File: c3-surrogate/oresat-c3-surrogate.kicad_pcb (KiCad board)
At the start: 2 copper layers, 99.8 x 94.6 mm, 72 parts, among them J1 J-SAMTEC-TFM-120-X1-XXX-D-RA, J2 Conn_01x04, J4 Conn_01x02_Socket, Q1 PMV45EN, Q3 NTR4101P, Q4 NTR2101P, Q5 DMP3050LVT-7, SW2 Slide Switch, SW3 OS203011MV9QS1, SW4 EG1218, U1 MAX892LEUA+T, U2 LTC4412xS6, U4 LTC4412xS6, U5 TS5A21366, U6 Trinket-M0

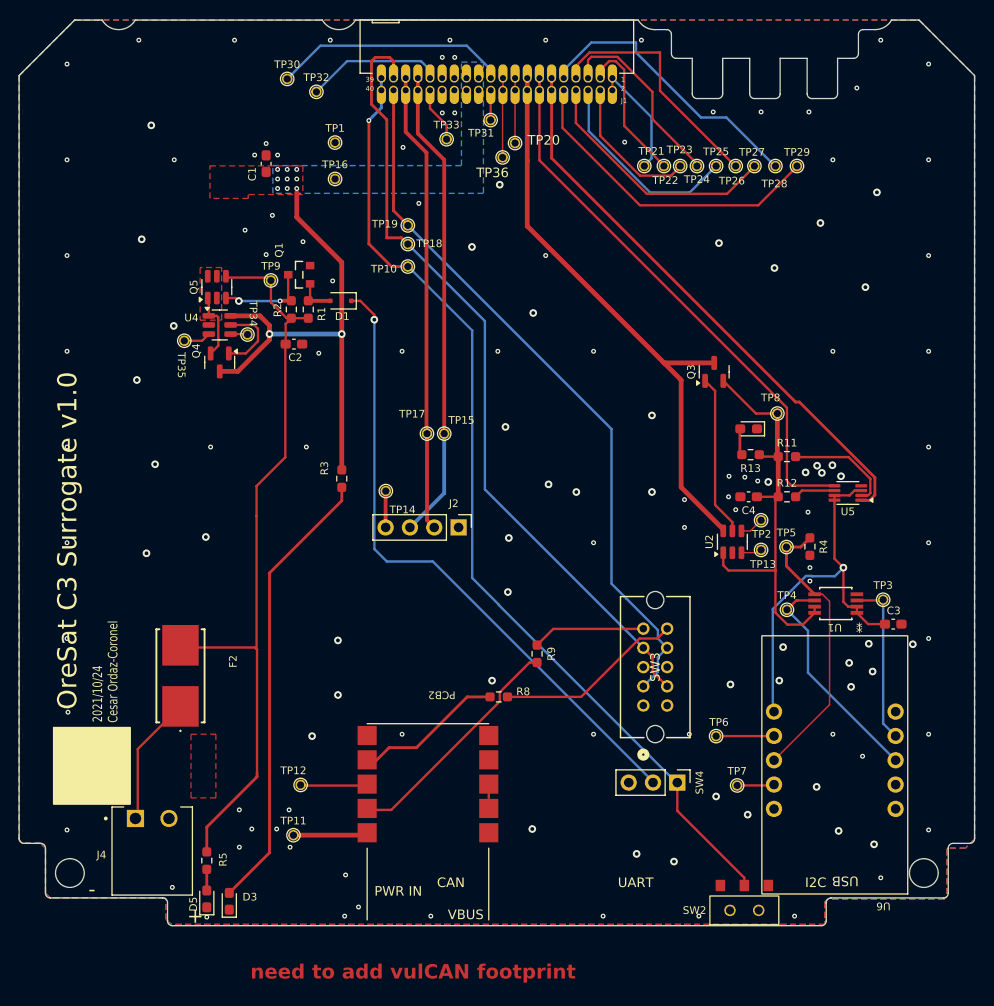
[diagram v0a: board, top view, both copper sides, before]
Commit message: made design review corrections to schematic and pcb
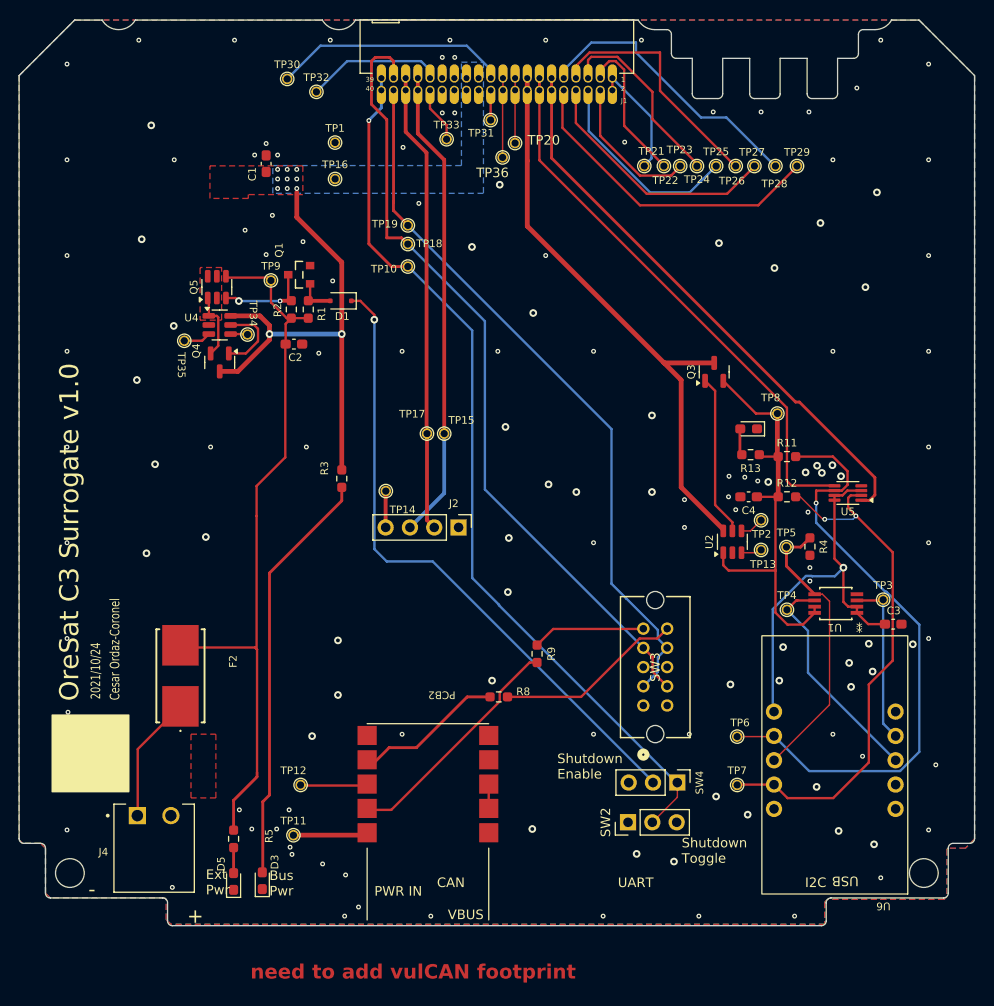
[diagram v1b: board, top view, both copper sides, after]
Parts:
- SW2: value Slide Switch -> EG1218; footprint S-CK-AYZ0102AGRLC-Slide-Switch:AYZ0102AGRLC -> Connector_PinHeader_2.54mm:PinHeader_1x03_P2.54mm_Vertical
- moved SW2 15.2 mm to (163.6, 139.2), turned to 90 degrees
- moved D3 4.07 mm to (125.4, 145.3)
- moved R5 3.60 mm to (122.4, 140.9)
- moved D5 3.34 mm to (122.4, 145.4)
- moved TP6 2.20 mm to (175.0, 130.2)
- moved J4 0.36 mm to (109.9, 146.5)
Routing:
- net Net-(U5-COM2): track 10.4 -> 64.3 mm, vias 0 -> 1
- net Net-(U5-COM1): track 15.2 -> 55.2 mm, vias 0 -> 2
- net ~{SD}: track 102.2 -> 93.8 mm
- net Net-(D3-A): track 47.2 -> 43.7 mm
- net Net-(Q5-S): track 79.0 -> 76.0 mm
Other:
- board text added: "Bus Pwr"
- board text added: "Ext Pwr"
- board text added: "Shutdown Enable"
- board text added: "Shutdown Toggle"

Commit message: edited via size, rearranged tracks
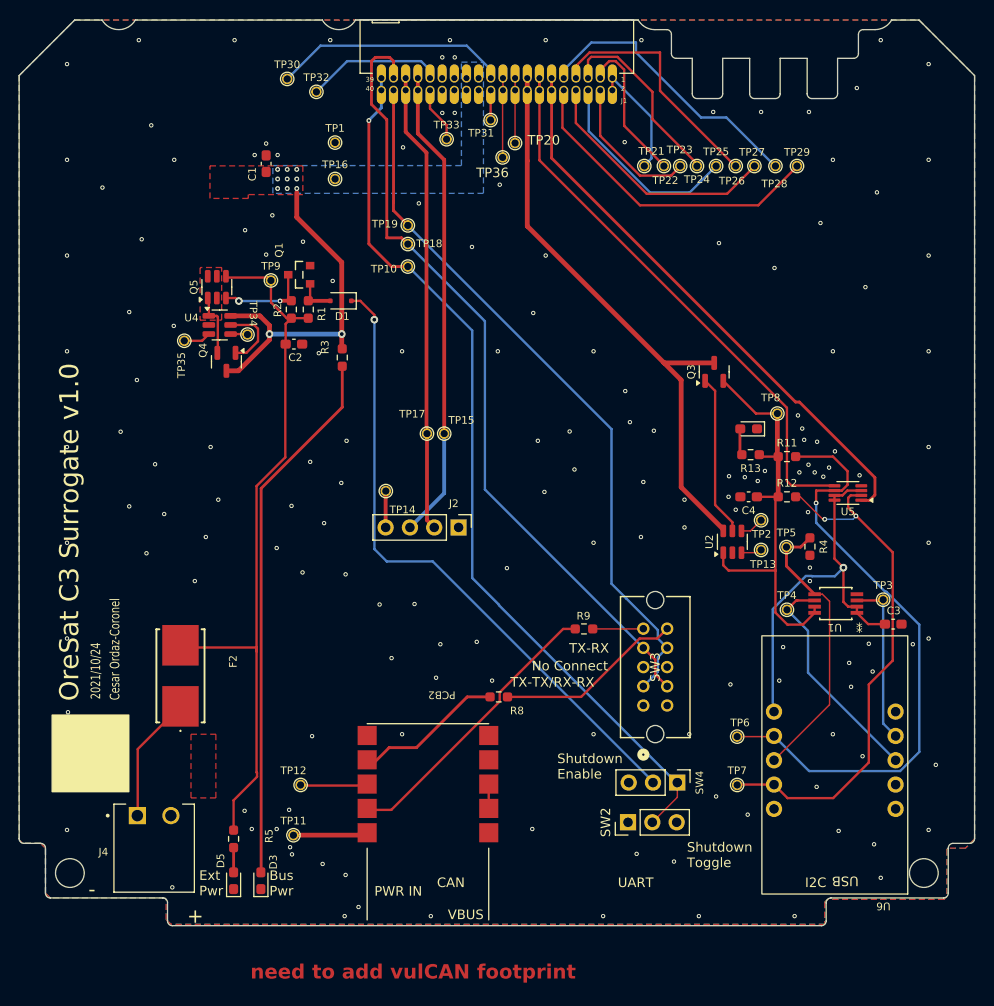
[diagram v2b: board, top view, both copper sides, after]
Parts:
- moved R3 12.7 mm to (133.8, 90.7)
- moved R9 5.55 mm to (159.0, 119.0), turned to 0 degrees
- moved Q4 0.70 mm to (121.7, 91.1)
- moved D3 0.15 mm to (125.2, 145.3)
- moved D5 0.08 mm to (122.4, 145.3)
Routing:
- net VBUS: track 51.0 -> 37.7 mm
- net Net-(D3-A): track 43.7 -> 56.4 mm
- net Net-(R9-Pad2): track 11.8 -> 5.30 mm
- net Net-(PCB2-RXD): track 24.7 -> 30.1 mm
- net Net-(Q4-G): track 7.91 -> 7.18 mm
- net GND: vias 134 -> 161
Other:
- board text added: "No Connect"
- board text added: "TX-RX"
- board text added: "TX-TX/RX-RX"

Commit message: fixed transistor that flipped
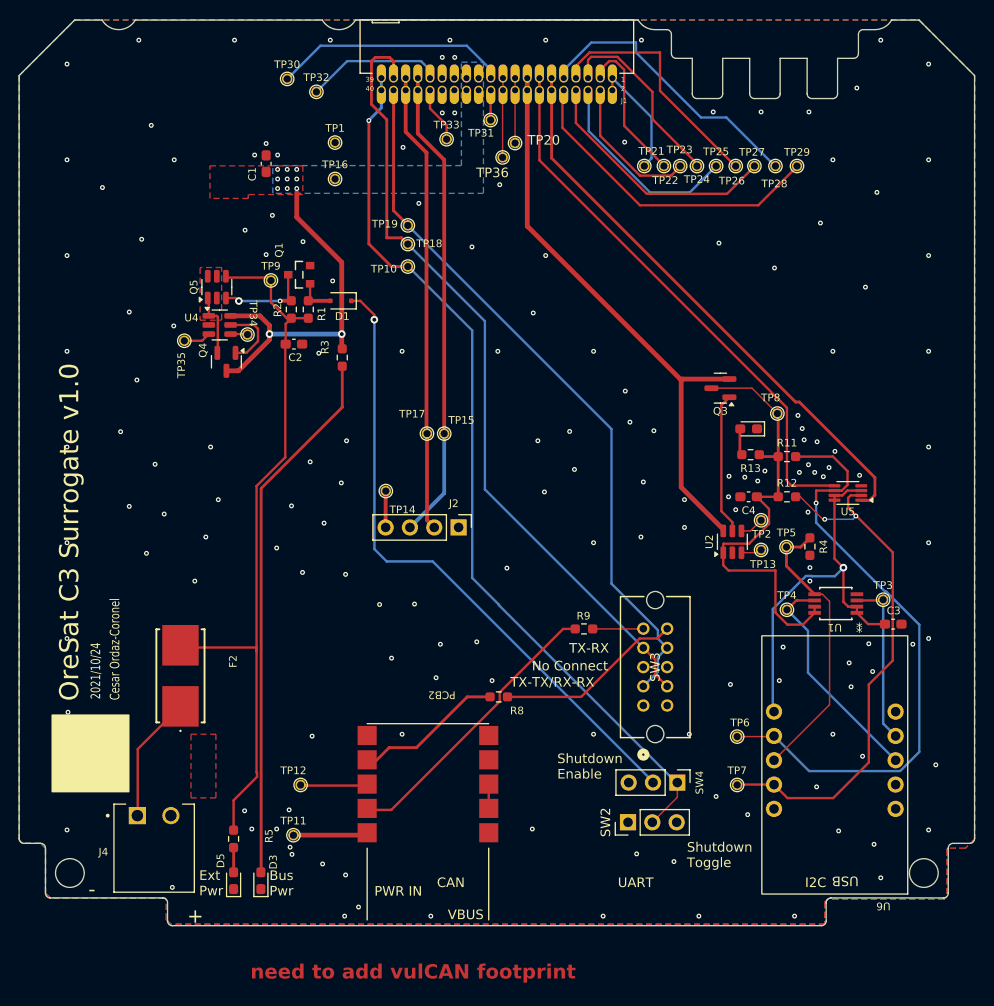
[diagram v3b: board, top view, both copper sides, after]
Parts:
- F2: value Fuse_Small -> 0155900DR
- Q4: value NTR2101P -> NTR4101P
- moved Q3 1.82 mm to (173.2, 93.8), turned to 180 degrees
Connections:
- C4 pad 1: Net-(Q3-S) -> Net-(Q3-D)
- Q3 pad 2: Net-(Q3-S) -> OPD_PWR
- Q3 pad 3: OPD_PWR -> Net-(Q3-D)
- R11 pad 1: Net-(Q3-S) -> Net-(Q3-D)
- R12 pad 1: Net-(Q3-S) -> Net-(Q3-D)
- R13 pad 1: Net-(Q3-S) -> Net-(Q3-D)
- TP8 pad 1: Net-(Q3-S) -> Net-(Q3-D)
- U1 pad 7: Net-(Q3-S) -> Net-(Q3-D)
- U1 pad 8: Net-(Q3-S) -> Net-(Q3-D)
- U2 pad 1: Net-(Q3-S) -> Net-(Q3-D)
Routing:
- net Net-(Q3-D): track 0.00 -> 48.6 mm
- net Net-(Q3-S): track 45.2 -> 0.00 mm
- net Net-(Q3-G): track 16.9 -> 14.8 mm

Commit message: added vulCAN
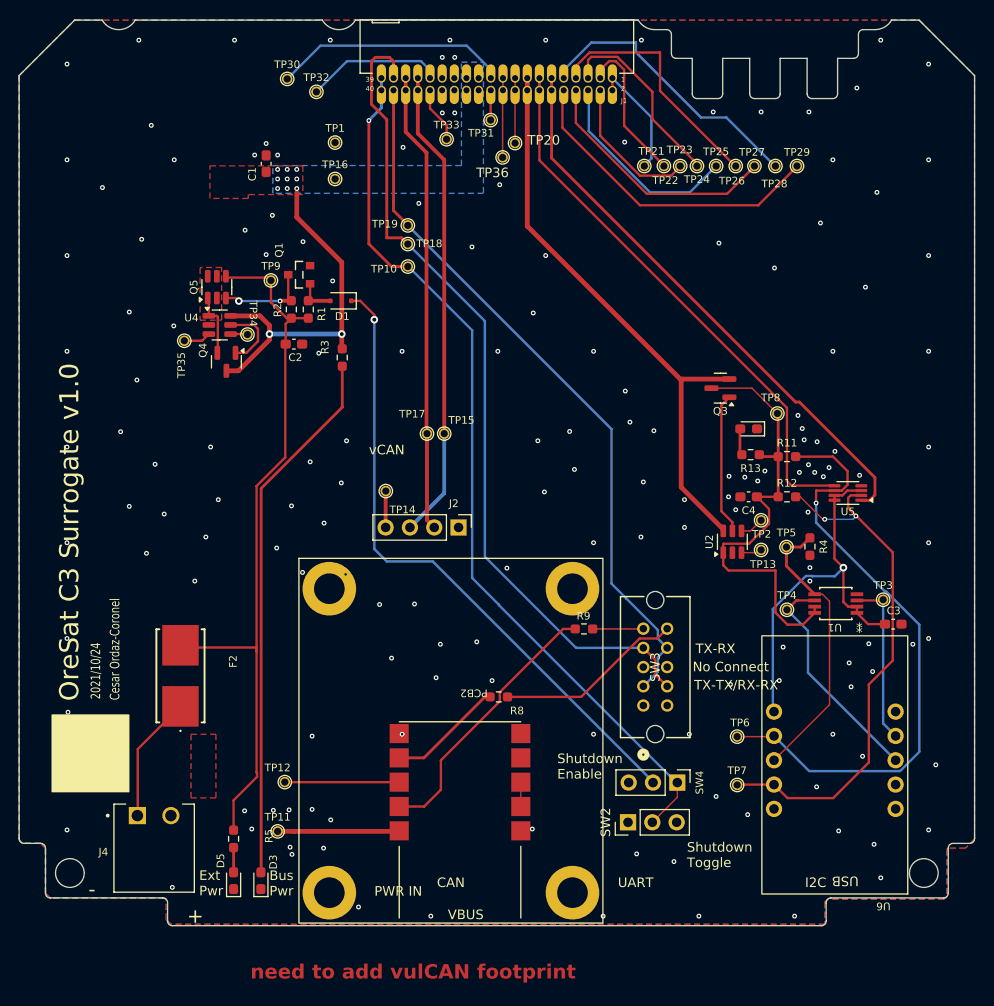
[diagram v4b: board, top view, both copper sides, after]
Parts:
- added vCAN: vulCAN, oresat-pcbs:vulCAN, F.Cu at (132.4, 114.8)
- moved PCB2 3.36 mm to (152.4, 149.7)
- moved TP11 1.70 mm to (127.0, 140.2)
- moved TP12 1.68 mm to (127.8, 135.0)
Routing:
- net Net-(PCB2-CTS#): track 7.75 -> 12.7 mm
- net Net-(PCB2-RTS#): track 7.01 -> 12.0 mm
- net C3-UART-TX: track 83.4 -> 87.5 mm
- net Net-(PCB2-TXD): track 15.6 -> 12.1 mm
- net Net-(PCB2-RXD): track 30.1 -> 28.4 mm

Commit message: fixed another transistor, and minor changes to pcb
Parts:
- moved Q4 0.55 mm to (121.1, 91.0), turned to 180 degrees
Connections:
- Q4 pad 2: Net-(Q4-S) -> VBUS
- Q4 pad 3: VBUS -> Net-(Q4-D)
- Q5 pad 1: Net-(Q4-S) -> Net-(Q4-D)
- Q5 pad 2: Net-(Q4-S) -> Net-(Q4-D)
- Q5 pad 5: Net-(Q4-S) -> Net-(Q4-D)
- Q5 pad 6: Net-(Q4-S) -> Net-(Q4-D)
- U4 pad 1: Net-(Q4-S) -> Net-(Q4-D)
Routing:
- net Net-(Q4-D): track 0.00 -> 7.81 mm
- net Net-(Q4-S): track 6.83 -> 0.00 mm
- net VBUS: track 37.7 -> 36.1 mm
- net Net-(PCB2-RXD): track 28.4 -> 27.2 mm
- net Net-(Q4-G): track 7.18 -> 6.02 mm
- net GND: vias 161 -> 164
- added copper zone on F.Cu, net Net-(Q4-D)
- removed copper zone on F.Cu, net Net-(Q4-S)

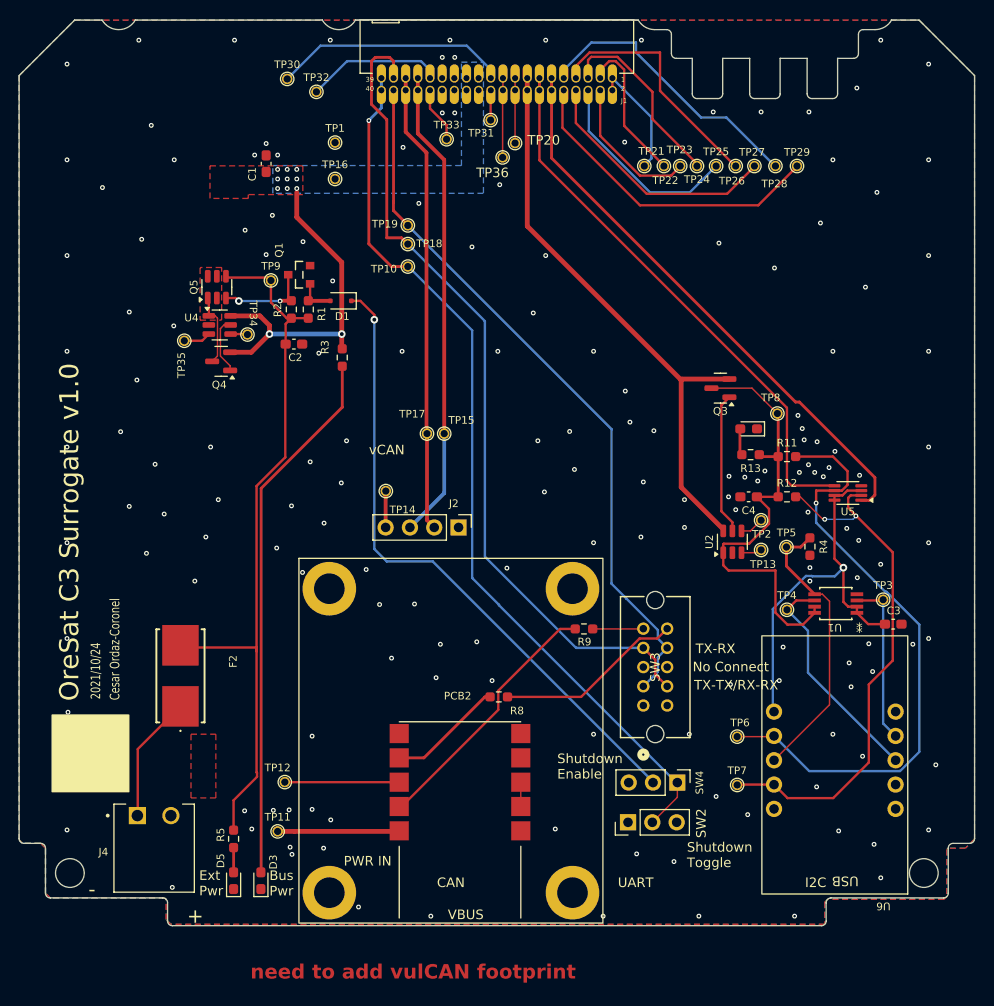
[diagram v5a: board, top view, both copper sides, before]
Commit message: edit pcb layout on left side of board (power connectors and sd switch)
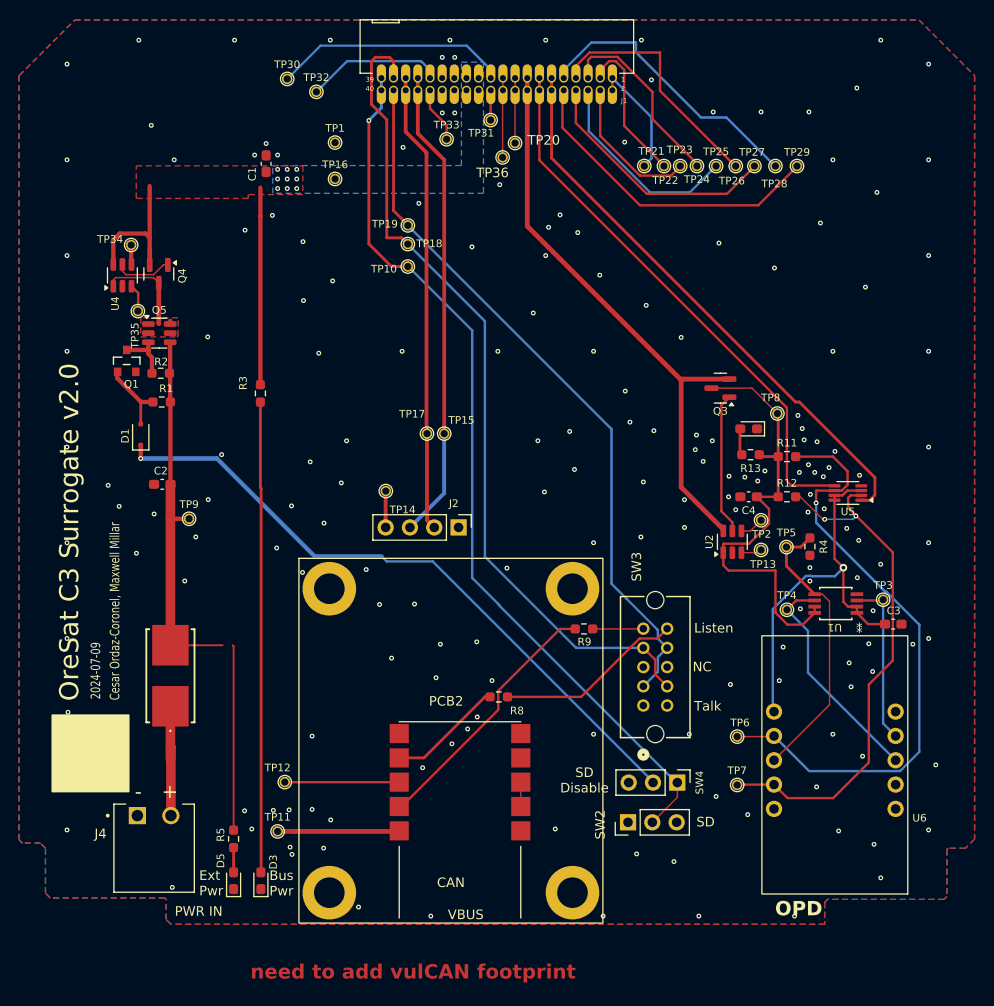
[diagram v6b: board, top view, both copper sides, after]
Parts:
- removed PCB1: ORESAT-CARD-V1.3-GENERIC-3RF, oresat-pcbs:ORESAT-CARD-V1.3-3RF
- J4: value Conn_01x02_Socket -> PHOENIX_1995499
- moved TP9 26.3 mm to (117.8, 107.5)
- moved D1 25.1 mm to (112.7, 98.7), turned to 90 degrees
- moved Q1 20.1 mm to (111.2, 91.0), turned to 0 degrees
- moved C2 20.1 mm to (115.0, 103.9), turned to 180 degrees
- moved R1 18.1 mm to (114.9, 95.3), turned to 180 degrees
- moved TP34 15.3 mm to (111.7, 78.9), turned to 0 degrees
- moved R2 15.2 mm to (114.8, 92.3), turned to 180 degrees
- moved U4 11.4 mm to (110.8, 82.1), turned to 90 degrees
- moved Q4 11.2 mm to (114.6, 81.9), turned to -90 degrees
- moved R3 9.34 mm to (125.2, 94.4)
- moved Q5 7.69 mm to (114.6, 88.1), turned to 0 degrees
- moved TP35 5.76 mm to (112.4, 85.8)
- moved F2 1.05 mm to (115.8, 123.9)
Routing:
- net Net-(Q5-S): track 76.0 -> 58.1 mm
- net Net-(D3-A): track 56.4 -> 49.2 mm
- net Net-(Q1-D): track 9.83 -> 5.68 mm, vias 2 -> 0
- net Net-(D1-A): track 4.48 -> 7.77 mm
- net Net-(Q4-D): track 7.81 -> 10.1 mm
- net Net-(D1-K): track 66.8 -> 69.0 mm
- net VBUS: track 36.1 -> 35.7 mm, vias 11 -> 9
- net GND: track 0.00 -> 0.05 mm, vias 164 -> 178
- removed copper zone on F.Cu, net (none)
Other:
- board outline removed
- board text added: "${ISSUE_DATE}"
- board text added: "Cesar Ordaz-Coronel, Maxwell Millar"
- board text added: "Listen"
- board text added: "NC"
- board text added: "OPD"
- board text added: "OreSat C3 Surrogate v${REVISION}"
- board text added: "SD"
- board text added: "SD Disable"
- board text added: "Talk"
- board text removed: "2021/10/24"
- board text removed: "Cesar Ordaz-Coronel"
- board text removed: "I2C"
- board text removed: "No Connect"
- board text removed: "OreSat C3 Surrogate v1.0"
- board text removed: "Shutdown Enable"
- board text removed: "Shutdown Toggle"
- board text removed: "TX-RX"
- board text removed: "TX-TX/RX-RX"
- board text removed: "UART"

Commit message: general changes
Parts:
- moved TP2 7.36 mm to (172.9, 101.9)
- moved TP13 6.83 mm to (171.1, 108.5)
- moved U2 6.22 mm to (170.1, 105.5)
- moved TP6 0.80 mm to (174.2, 130.2)
- moved U1 0.74 mm to (184.6, 116.6)
- moved TP4 0.71 mm to (180.1, 116.3)
- moved D13 0.28 mm to (176.4, 98.3)
- moved R13 0.20 mm to (176.4, 101.0)
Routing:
- net OPD_PWR: track 60.9 -> 54.6 mm
- net Net-(U1-IN): track 40.2 -> 34.0 mm, vias 1 -> 0
- net Net-(U5-COM1): track 55.2 -> 51.3 mm
- net Net-(U5-COM2): track 64.3 -> 60.6 mm
- net Net-(Q3-G): track 14.8 -> 11.4 mm
- net OPD_SCL: track 58.0 -> 55.3 mm
- net /OPD_ISET: track 29.9 -> 32.3 mm
- net Net-(U2-STAT): track 2.51 -> 3.35 mm
- net /OPD_~{ENABLE}: track 17.5 -> 18.3 mm
- net Net-(PCB2-RXD): track 27.2 -> 27.9 mm
- net Net-(Q3-D): track 48.6 -> 48.1 mm
- net GND: vias 178 -> 186
- added copper zone on F.Cu, net Net-(Q5-S)
